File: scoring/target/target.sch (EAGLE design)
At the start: 11 parts, among them J1 AVRISP6_COMPACT, U1 ATTINY85-20SU

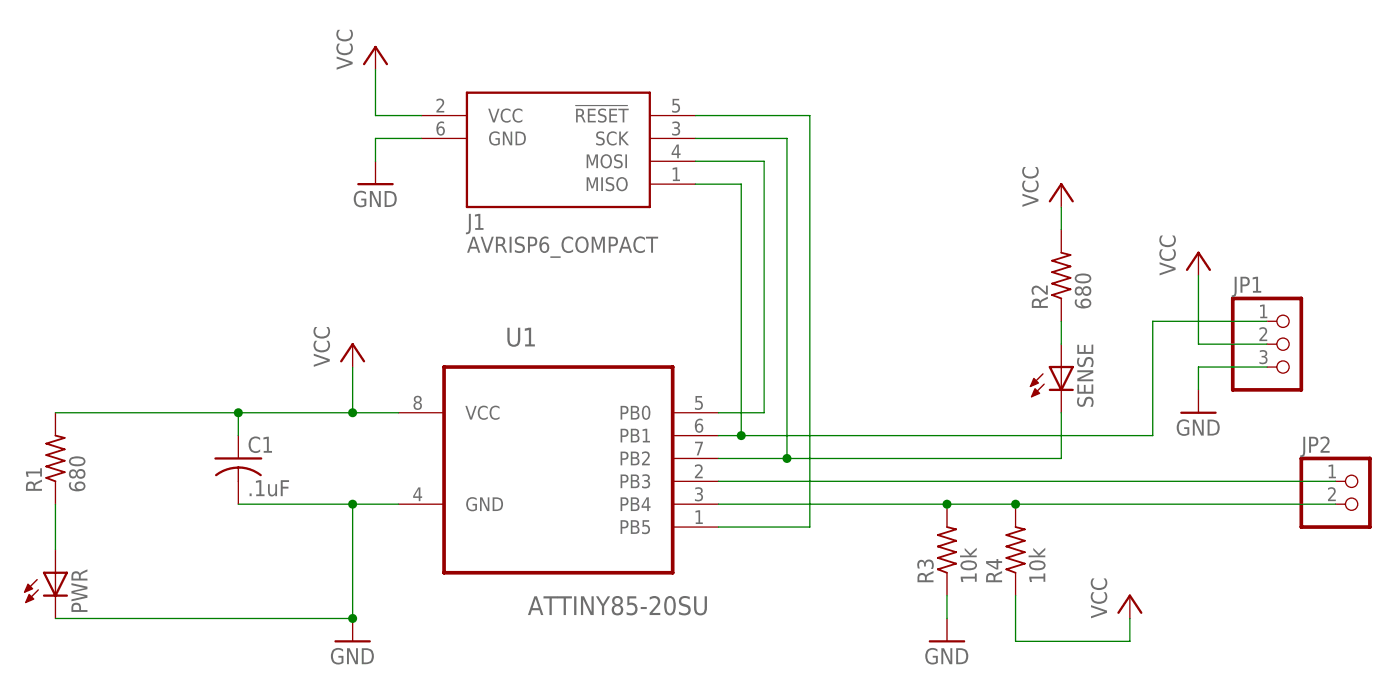
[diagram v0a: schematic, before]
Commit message: Update panel board with piezo load resistors.
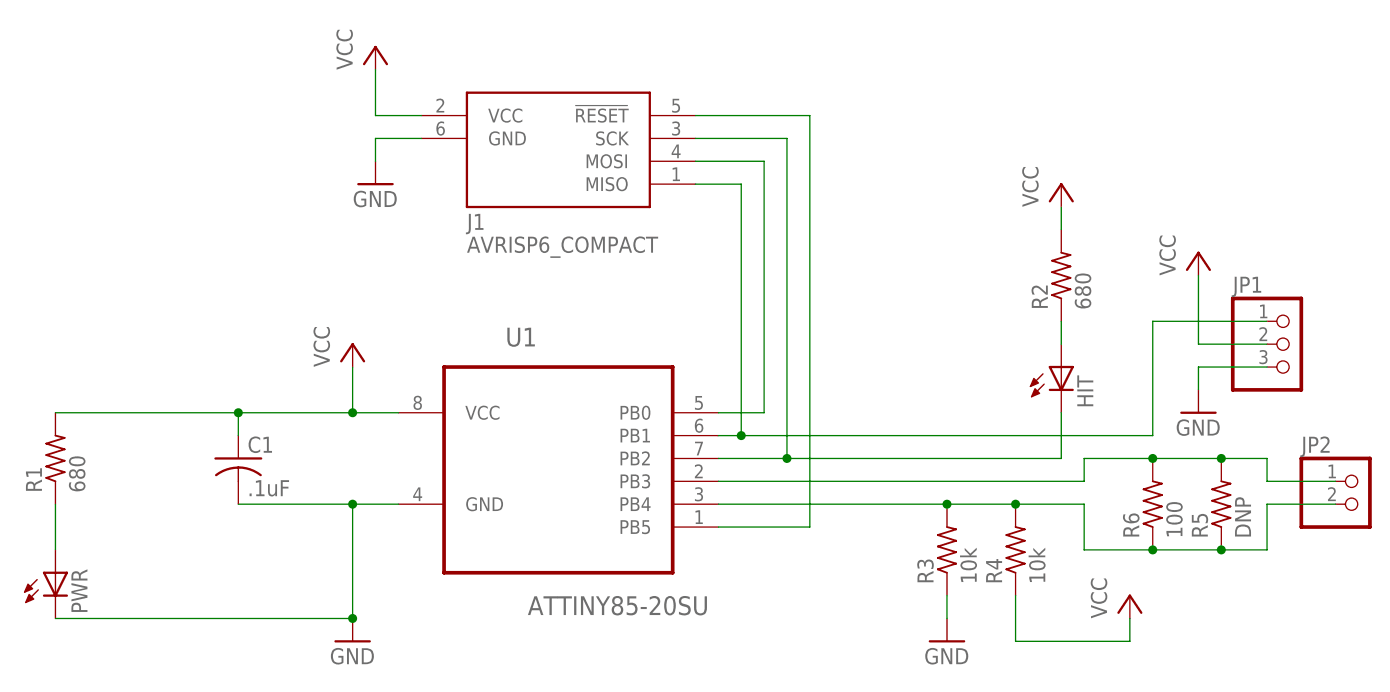
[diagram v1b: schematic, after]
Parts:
- added R5: DNP, rcl:R-US_R0805
- added R6: 100, rcl:R-US_R0805
- renumbered SENSE to HIT
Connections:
- net N$3: now also R5.1, R6.1
- net N$6: now also R5.2, R6.2
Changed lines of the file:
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@@
 <attribute name="DPN" value="160-1469-1-ND"/>
 </part>
-<part name="SENSE" library="led" deviceset="LED" device="SML0805">
+<part name="HIT" library="led" deviceset="LED" device="SML0805">
 <attribute name="DPN" value="160-1414-1-ND"/>
 </part>
@@
 <part name="P+5" library="supply1" deviceset="VCC" device=""/>
 <part name="JP2" library="pinhead" deviceset="PINHD-1X2" device=""/>
+<part name="R5" library="rcl" deviceset="R-US_" device="R0805" value="DNP"/>
+<part name="R6" library="rcl" deviceset="R-US_" device="R0805" value="100">
+<attribute name="P100ACT-ND" value=""/>
+</part>
 </parts>
 <sheets>
@@
 <attribute name="DPN" x="-22.86" y="27.94" size="1.778" layer="96" display="off"/>
 </instance>
-<instance part="SENSE" gate="G$1" x="88.9" y="50.8">
+<instance part="HIT" gate="G$1" x="88.9" y="50.8">
 <attribute name="DPN" x="88.9" y="50.8" size="1.778" layer="96" display="off"/>
 </instance>
@@
 <instance part="P+5" gate="VCC" x="104.14" y="63.5"/>
 <instance part="JP2" gate="G$1" x="121.92" y="35.56"/>
+<instance part="R5" gate="G$1" x="106.68" y="35.56" rot="R90"/>
+<instance part="R6" gate="G$1" x="99.06" y="35.56" rot="R90">
+<attribute name="P100ACT-ND" x="99.06" y="35.56" size="1.778" layer="96" rot="R90" display="off"/>
+</instance>
 </instances>
 <busses>
@@
 <wire x1="50.8" y1="35.56" x2="76.2" y2="35.56" width="0.1524" layer="91"/>
 <junction x="76.2" y="35.56"/>
+<wire x1="83.82" y1="35.56" x2="91.44" y2="35.56" width="0.1524" layer="91"/>
+<wire x1="91.44" y1="35.56" x2="91.44" y2="30.48" width="0.1524" layer="91"/>
 <junction x="83.82" y="35.56"/>
+<pinref part="R6" gate="G$1" pin="1"/>
+<wire x1="91.44" y1="30.48" x2="99.06" y2="30.48" width="0.1524" layer="91"/>
+<pinref part="R5" gate="G$1" pin="1"/>
+<wire x1="99.06" y1="30.48" x2="106.68" y2="30.48" width="0.1524" layer="91"/>
+<junction x="99.06" y="30.48"/>
+<wire x1="106.68" y1="30.48" x2="111.76" y2="30.48" width="0.1524" layer="91"/>
+<junction x="106.68" y="30.48"/>
+<wire x1="111.76" y1="30.48" x2="111.76" y2="35.56" width="0.1524" layer="91"/>
 <pinref part="JP2" gate="G$1" pin="2"/>
-<wire x1="83.82" y1="35.56" x2="119.38" y2="35.56" width="0.1524" layer="91"/>
+<wire x1="111.76" y1="35.56" x2="119.38" y2="35.56" width="0.1524" layer="91"/>
 </segment>
 </net>
@@
 <segment>
 <pinref part="U1" gate="A" pin="PB2"/>
-<pinref part="SENSE" gate="G$1" pin="C"/>
+<pinref part="HIT" gate="G$1" pin="C"/>
 <wire x1="50.8" y1="40.64" x2="58.42" y2="40.64" width="0.1524" layer="91"/>
 <wire x1="58.42" y1="40.64" x2="88.9" y2="40.64" width="0.1524" layer="91"/>
@@
 <segment>
 <pinref part="R2" gate="G$1" pin="1"/>
-<pinref part="SENSE" gate="G$1" pin="A"/>
+<pinref part="HIT" gate="G$1" pin="A"/>
 <wire x1="88.9" y1="55.88" x2="88.9" y2="53.34" width="0.1524" layer="91"/>
-</segment>
-</net>
-<net name="N$6" class="0">
-<segment>
-<pinref part="U1" gate="A" pin="PB3"/>
-<wire x1="50.8" y1="38.1" x2="119.38" y2="38.1" width="0.1524" layer="91"/>
-<pinref part="JP2" gate="G$1" pin="1"/>
 </segment>
 </net>
@@
 </segment>
 </net>
+<net name="N$6" class="0">
+<segment>
+<pinref part="U1" gate="A" pin="PB3"/>
+<wire x1="50.8" y1="38.1" x2="91.44" y2="38.1" width="0.1524" layer="91"/>
+<wire x1="91.44" y1="38.1" x2="91.44" y2="40.64" width="0.1524" layer="91"/>
+<pinref part="R6" gate="G$1" pin="2"/>
+<wire x1="91.44" y1="40.64" x2="99.06" y2="40.64" width="0.1524" layer="91"/>
+<pinref part="R5" gate="G$1" pin="2"/>
+<wire x1="99.06" y1="40.64" x2="106.68" y2="40.64" width="0.1524" layer="91"/>
+<junction x="99.06" y="40.64"/>
+<wire x1="106.68" y1="40.64" x2="111.76" y2="40.64" width="0.1524" layer="91"/>
+<wire x1="111.76" y1="40.64" x2="111.76" y2="38.1" width="0.1524" layer="91"/>
+<junction x="106.68" y="40.64"/>
+<pinref part="JP2" gate="G$1" pin="1"/>
+<wire x1="111.76" y1="38.1" x2="119.38" y2="38.1" width="0.1524" layer="91"/>
+</segment>
+</net>
